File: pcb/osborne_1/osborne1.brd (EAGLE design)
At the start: 40 x 97 mm, 11 parts, among them J2 ATX24RH

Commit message: cleanup
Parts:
- moved JP1 2.24 mm to (6.97, 79.2)
- moved JP2 2.24 mm to (6.97, 67.7)
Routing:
- net +5V: track 69.2 -> 79.6 mm
- net +12V: track 85.0 -> 83.1 mm
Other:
- board text added: "12VDC"
- board text added: "Center Positive"

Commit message: cleanup
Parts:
- moved JP4 0.76 mm to (5.46, 21.2)
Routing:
- net +5V: track 79.6 -> 78.9 mm
- net +12V: track 83.1 -> 82.6 mm
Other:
- board text added: "12V"
- board text added: "5V"
- board text added: "Fan Voltage"
- board text added: "PD1 dekuNukem APR 2023"
- board text removed: "12"
- board text removed: "5"
- board text removed: "PT1 dekuNukem APR 2023"
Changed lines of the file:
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@@
 <grid distance="5" unitdist="mil" unit="mil" style="lines" multiple="1" display="no" altdistance="1" altunitdist="mil" altunit="mil"/>
 <layers>
-<layer number="1" name="Top" color="4" fill="1" visible="no" active="yes"/>
+<layer number="1" name="Top" color="4" fill="1" visible="yes" active="yes"/>
 <layer number="2" name="Route2" color="16" fill="1" visible="no" active="no"/>
 <layer number="3" name="Route3" color="17" fill="1" visible="no" active="no"/>
@@
 <layer number="19" name="Unrouted" color="6" fill="1" visible="yes" active="yes"/>
 <layer number="20" name="Dimension" color="24" fill="1" visible="yes" active="yes"/>
-<layer number="21" name="tPlace" color="7" fill="1" visible="no" active="yes"/>
-<layer number="22" name="bPlace" color="7" fill="1" visible="no" active="yes"/>
-<layer number="23" name="tOrigins" color="15" fill="1" visible="no" active="yes"/>
+<layer number="21" name="tPlace" color="7" fill="1" visible="yes" active="yes"/>
+<layer number="22" name="bPlace" color="7" fill="1" visible="yes" active="yes"/>
+<layer number="23" name="tOrigins" color="15" fill="1" visible="yes" active="yes"/>
 <layer number="24" name="bOrigins" color="15" fill="1" visible="yes" active="yes"/>
-<layer number="25" name="tNames" color="7" fill="1" visible="no" active="yes"/>
-<layer number="26" name="bNames" color="7" fill="1" visible="no" active="yes"/>
-<layer number="27" name="tValues" color="7" fill="1" visible="no" active="yes"/>
-<layer number="28" name="bValues" color="7" fill="1" visible="no" active="yes"/>
+<layer number="25" name="tNames" color="7" fill="1" visible="yes" active="yes"/>
+<layer number="26" name="bNames" color="7" fill="1" visible="yes" active="yes"/>
+<layer number="27" name="tValues" color="7" fill="1" visible="yes" active="yes"/>
+<layer number="28" name="bValues" color="7" fill="1" visible="yes" active="yes"/>
 <layer number="29" name="tStop" color="7" fill="3" visible="no" active="yes"/>
 <layer number="30" name="bStop" color="7" fill="6" visible="no" active="yes"/>
@@
 <layer number="37" name="tTest" color="7" fill="1" visible="no" active="yes"/>
 <layer number="38" name="bTest" color="7" fill="1" visible="no" active="yes"/>
-<layer number="39" name="tKeepout" color="4" fill="11" visible="no" active="yes"/>
+<layer number="39" name="tKeepout" color="4" fill="11" visible="yes" active="yes"/>
 <layer number="40" name="bKeepout" color="1" fill="11" visible="yes" active="yes"/>
-<layer number="41" name="tRestrict" color="4" fill="10" visible="no" active="yes"/>
+<layer number="41" name="tRestrict" color="4" fill="10" visible="yes" active="yes"/>
 <layer number="42" name="bRestrict" color="1" fill="10" visible="yes" active="yes"/>
 <layer number="43" name="vRestrict" color="2" fill="10" visible="no" active="yes"/>
@@
 <layer number="49" name="Reference" color="7" fill="1" visible="no" active="yes"/>
 <layer number="50" name="dxf" color="7" fill="1" visible="no" active="no"/>
-<layer number="51" name="tDocu" color="7" fill="1" visible="no" active="yes"/>
-<layer number="52" name="bDocu" color="7" fill="1" visible="no" active="yes"/>
+<layer number="51" name="tDocu" color="7" fill="1" visible="yes" active="yes"/>
+<layer number="52" name="bDocu" color="7" fill="1" visible="yes" active="yes"/>
 <layer number="53" name="tGND_GNDA" color="7" fill="1" visible="no" active="no"/>
 <layer number="54" name="bGND_GNDA" color="7" fill="1" visible="no" active="no"/>
@@
 <wire x1="0" y1="94.46" x2="0" y2="2.54" width="0" layer="20"/>
 <wire x1="0" y1="2.54" x2="2.54" y2="0" width="0" layer="20" curve="90"/>
-<text x="11.557" y="5.715" size="2.1844" layer="25" distance="35" align="center">picoRC.com</text>
+<text x="11.557" y="5.588" size="2.54" layer="25" distance="35" align="center">picoRC.com</text>
 <text x="28.2636" y="12.5134" size="2.1844" layer="25" distance="35" align="center">Osborne 1
 PicoPSU Adaptor</text>
-<text x="9.922" y="91.722" size="1.4224" layer="25" distance="30" align="center">PT1 dekuNukem
+<text x="9.922" y="91.722" size="1.4224" layer="25" distance="30" align="center">PD1 dekuNukem
 APR 2023</text>
 <text x="4.699" y="50.546" size="1.9304" layer="25" distance="35" rot="R90" align="center">FUSE
@@
 <text x="12.233" y="68.942" size="1.6764" layer="26" rot="MR0" align="center">RED</text>
 <text x="11.725" y="71.482" size="1.6764" layer="26" rot="MR0" align="center">NC</text>
-<text x="1.632" y="18.777" size="1.778" layer="25" align="center">12</text>
-<text x="1.505" y="23.73" size="1.778" layer="25" align="center">5</text>
+<text x="4.845" y="14.967" size="1.778" layer="25" rot="R90" align="center">12V</text>
+<text x="5.442" y="27.07" size="1.778" layer="25" rot="R270" align="center">5V</text>
 <text x="15.132" y="8.363" size="1.778" layer="26" rot="MR90" align="center">GND</text>
 <text x="12.6428" y="8.363" size="1.778" layer="26" rot="MR90" align="center">VCC</text>
@@
 <text x="33.528" y="87.376" size="2.1844" layer="25" distance="35" align="center">Center
 Positive</text>
+<text x="2.667" y="80.391" size="1.778" layer="25" align="center">12V</text>
+<text x="2.667" y="75.438" size="1.778" layer="25" align="center">5V</text>
+<text x="2.667" y="77.851" size="1.778" layer="25" align="center">GND</text>
+<text x="2.667" y="83.058" size="1.778" layer="25" align="center">NC</text>
+<text x="2.667" y="68.961" size="1.778" layer="25" align="center">12V</text>
+<text x="2.667" y="64.008" size="1.778" layer="25" align="center">5V</text>
+<text x="2.667" y="66.421" size="1.778" layer="25" align="center">GND</text>
+<text x="2.667" y="71.628" size="1.778" layer="25" align="center">NC</text>
+<text x="2.14" y="20.847" size="1.778" layer="25" rot="R270" align="center">Fan Voltage</text>
 </plain>
 <attributes>
@@
 <element name="U$2" library="atx_power_control" package="FUSE_HOLDER_3IN1" value="CAR_FUSE_HOLDER3IN1" x="11.43" y="29.591" smashed="yes" rot="R90"/>
 <element name="J2" library="macse" package="ATX24_RIGHT_ANGLE" value="ATX24RH" x="31" y="43" smashed="yes" rot="R90"/>
-<element name="JP4" library="pinhead" library_urn="urn:adsk.eagle:library:325" package="1X03" package3d_urn="urn:adsk.eagle:package:22458/2" value="" x="4.699" y="21.209" smashed="yes" rot="R90">
-<attribute name="POPULARITY" value="92" x="4.699" y="21.209" size="1.778" layer="27" rot="R90" display="off"/>
-<attribute name="VALUE" x="7.874" y="17.399" size="1.27" layer="27" rot="R90"/>
+<element name="JP4" library="pinhead" library_urn="urn:adsk.eagle:library:325" package="1X03" package3d_urn="urn:adsk.eagle:package:22458/2" value="" x="5.461" y="21.209" smashed="yes" rot="R90">
+<attribute name="POPULARITY" value="92" x="5.461" y="21.209" size="1.778" layer="27" rot="R90" display="off"/>
+<attribute name="VALUE" x="8.636" y="17.399" size="1.27" layer="27" rot="R90"/>
 </element>
 <element name="JP3" library="appleii" package="1X04" value="" x="11.303" y="13.716" smashed="yes" rot="MR0"/>
@@
 <wire x1="14.224" y1="40.259" x2="15.494" y2="38.989" width="0.6096" layer="16"/>
 <wire x1="15.494" y1="38.989" x2="15.494" y2="33.655" width="0.6096" layer="16"/>
-<wire x1="5.588" y1="23.749" x2="4.699" y2="23.749" width="0.6096" layer="16"/>
+<wire x1="5.588" y1="23.749" x2="5.461" y2="23.749" width="0.6096" layer="16"/>
 <wire x1="6.096" y1="55.663" x2="6.096" y2="42.037" width="0.6096" layer="16"/>
 <wire x1="15.494" y1="33.655" x2="5.588" y2="23.749" width="0.6096" layer="16"/>
@@
 <contactref element="JP2" pad="3"/>
 <wire x1="9.68" y1="36.641" x2="9.361" y2="36.322" width="1.778" layer="16"/>
-<wire x1="9.361" y1="36.322" x2="2.159" y2="36.322" width="1.778" layer="16"/>
 <wire x1="6.969" y1="80.423" x2="4.937" y2="80.423" width="1.778" layer="16"/>
 <wire x1="13.18" y1="36.641" x2="9.68" y2="36.641" width="1.778" layer="16"/>
-<wire x1="4.699" y1="18.669" x2="2.032" y2="18.669" width="1.016" layer="16"/>
-<wire x1="2.032" y1="18.669" x2="1.778" y2="18.923" width="1.016" layer="16"/>
-<wire x1="1.778" y1="18.923" x2="1.778" y2="35.941" width="1.016" layer="16"/>
-<wire x1="1.778" y1="35.941" x2="1.905" y2="36.068" width="1.016" layer="16"/>
-<wire x1="2.159" y1="36.322" x2="2.905" y2="37.068" width="1.016" layer="16"/>
-<wire x1="1.905" y1="36.068" x2="2.159" y2="36.322" width="1.016" layer="16"/>
 <wire x1="4.937" y1="80.423" x2="2.905" y2="78.391" width="1.778" layer="16"/>
 <wire x1="2.905" y1="78.391" x2="2.905" y2="68.993" width="1.778" layer="16"/>
 <wire x1="2.905" y1="68.993" x2="2.905" y2="37.068" width="1.778" layer="16"/>
 <wire x1="6.969" y1="68.993" x2="2.905" y2="68.993" width="1.778" layer="16"/>
+<wire x1="9.68" y1="36.641" x2="3.332" y2="36.641" width="1.778" layer="16"/>
+<wire x1="3.332" y1="36.641" x2="2.905" y2="37.068" width="1.778" layer="16"/>
+<wire x1="5.461" y1="18.669" x2="3.048" y2="18.669" width="1.016" layer="16"/>
+<wire x1="3.048" y1="18.669" x2="2.286" y2="19.431" width="1.016" layer="16"/>
+<wire x1="2.286" y1="19.431" x2="2.286" y2="36.449" width="1.016" layer="16"/>
+<wire x1="2.286" y1="36.449" x2="2.905" y2="37.068" width="1.016" layer="16"/>
 </signal>
 <signal name="N$2">
 <contactref element="JP3" pad="2"/>
 <contactref element="JP4" pad="2"/>
-<wire x1="4.699" y1="21.209" x2="6.604" y2="21.209" width="1.016" layer="16"/>
-<wire x1="6.604" y1="21.209" x2="12.573" y2="15.24" width="1.016" layer="16"/>
-<wire x1="12.573" y1="15.24" x2="12.573" y2="13.716" width="1.016" layer="16"/>
+<wire x1="5.461" y1="21.209" x2="7.112" y2="21.209" width="1.016" layer="16"/>
+<wire x1="7.112" y1="21.209" x2="12.573" y2="15.748" width="1.016" layer="16"/>
+<wire x1="12.573" y1="15.748" x2="12.573" y2="13.716" width="1.016" layer="16"/>
 </signal>
 <signal name="N$1">

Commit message: finishing touches
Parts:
- added LED1, LED2: (no value), SparkFun-LED:LED_3MM
- added R1, R2: (no value), adafruit:0207/2V
- moved U$2 0.51 mm to (10.9, 29.6)
- moved U$8 0.51 mm to (10.9, 50.8)
- moved JP4 0.25 mm to (5.21, 21.2)
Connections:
- new net N$3: LED1.K, R2.1
- new net N$4: LED2.K, R1.1
- net +12V: now also LED2.A
- net +5V: now also LED1.A
- net GND: now also R1.2, R2.2
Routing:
- net +12V: track 82.6 -> 88.7 mm
- net +5V: track 78.9 -> 82.5 mm
- net N$3: track 0.00 -> 3.30 mm
- net N$4: track 0.00 -> 2.92 mm
- net N$8: track 37.7 -> 38.4 mm
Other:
- board text added: "+"

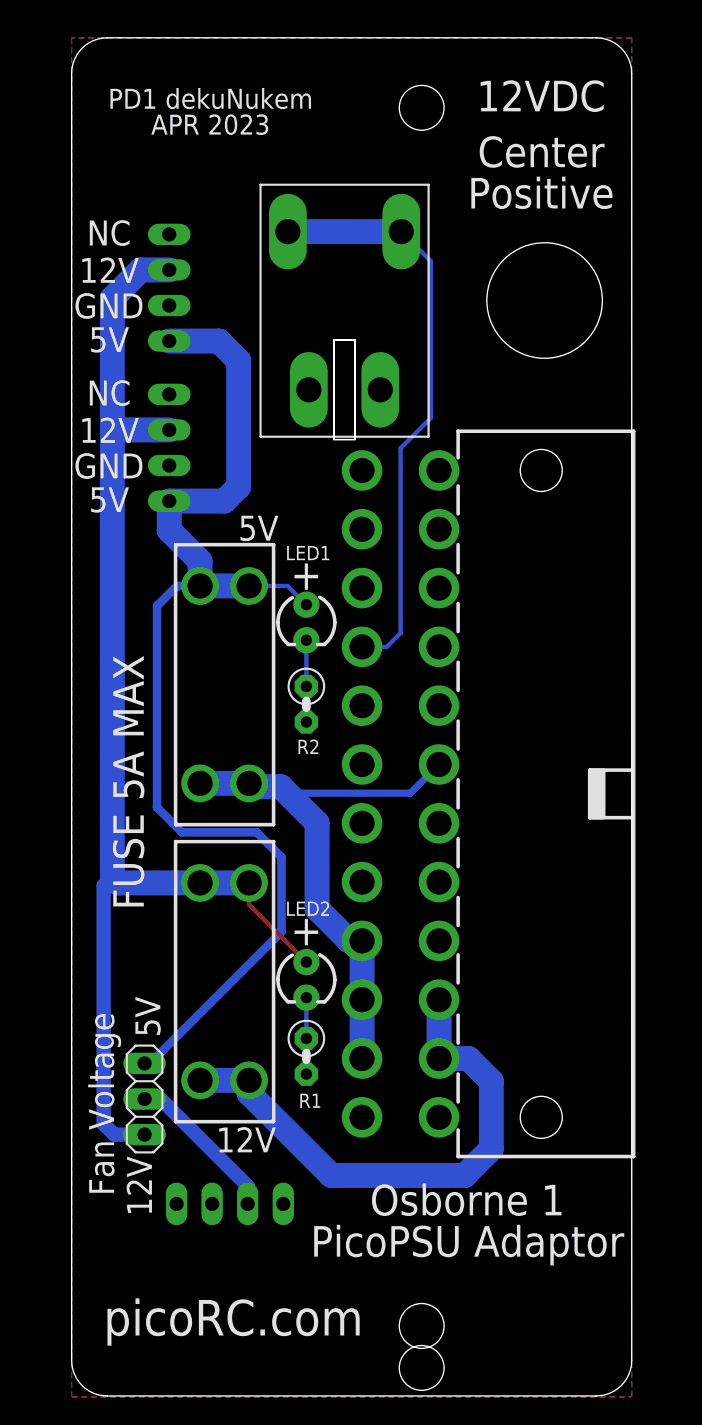
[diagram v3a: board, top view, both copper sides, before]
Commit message: added one more power connector, added decoupling cap
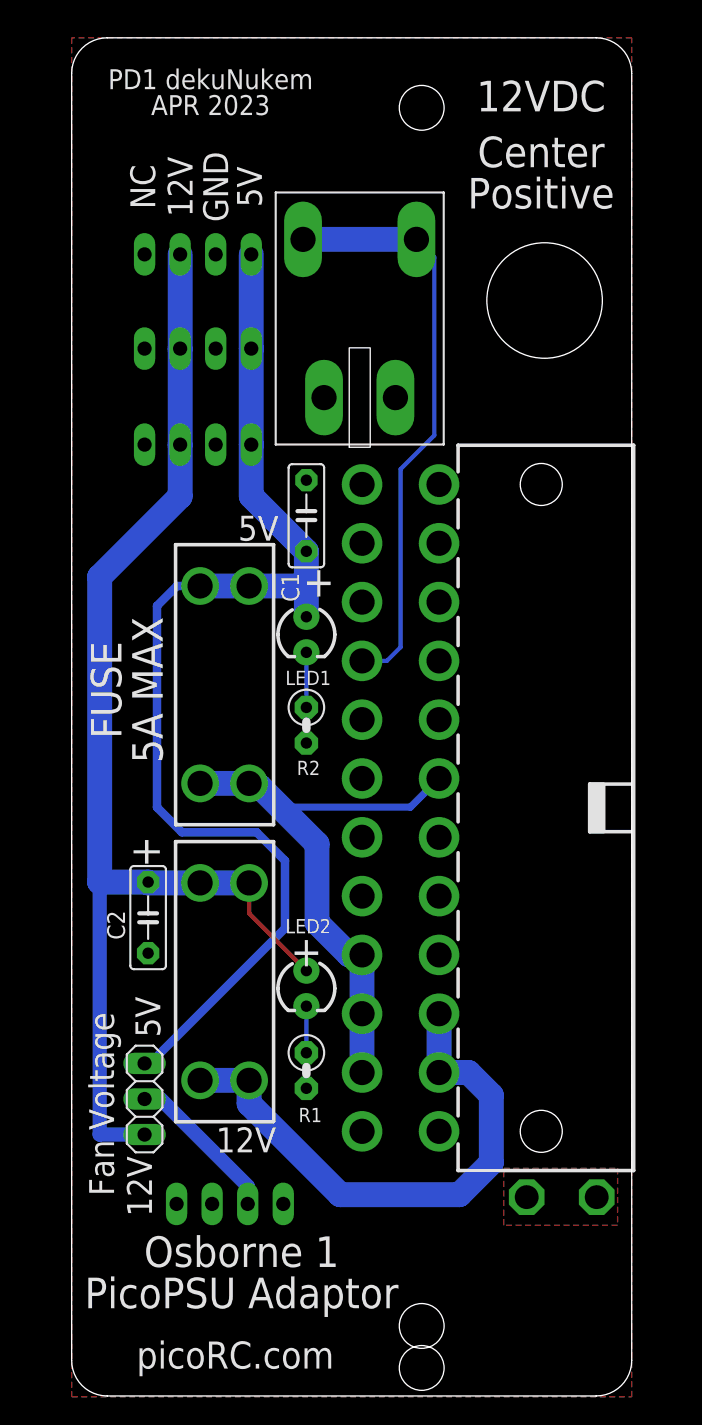
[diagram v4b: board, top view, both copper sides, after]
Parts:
- added C1, C2: (no value), capacitor-wima:C5B2.5
- added JP5: (no value), appleii:1X04
- added TP1, TP2: PTR1PAD1-17, testpad:P1-17
- moved JP2 7.37 mm to (9.02, 74.8), turned to 0 degrees
- moved JP1 3.14 mm to (9.02, 81.5), turned to 0 degrees
- moved R2 1.50 mm to (16.8, 47.9)
- moved U$4 1.22 mm to (20.6, 77.0)
- moved R1 1.02 mm to (16.8, 23.2)
- moved J2 1.00 mm to (31.0, 42.0)
- moved LED1 0.86 mm to (16.8, 54.4)
- moved LED2 0.61 mm to (16.8, 29.1)
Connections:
- net +12V: now also C2.1, JP5.3
- net +5V: now also C1.1, JP5.1
- net GND: now also C1.2, C2.2, JP5.2, TP1.TP, TP2.TP
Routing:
- net +12V: track 88.7 -> 87.1 mm
- net N$8: track 38.4 -> 39.5 mm
- net N$3: track 3.30 -> 3.94 mm
- net N$6: track 42.1 -> 42.6 mm
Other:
- outline, holes or cut-outs redrawn
- board text removed: "RED: 12V ORANGE: GND YELLOW: 5V"

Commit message: changed oritation
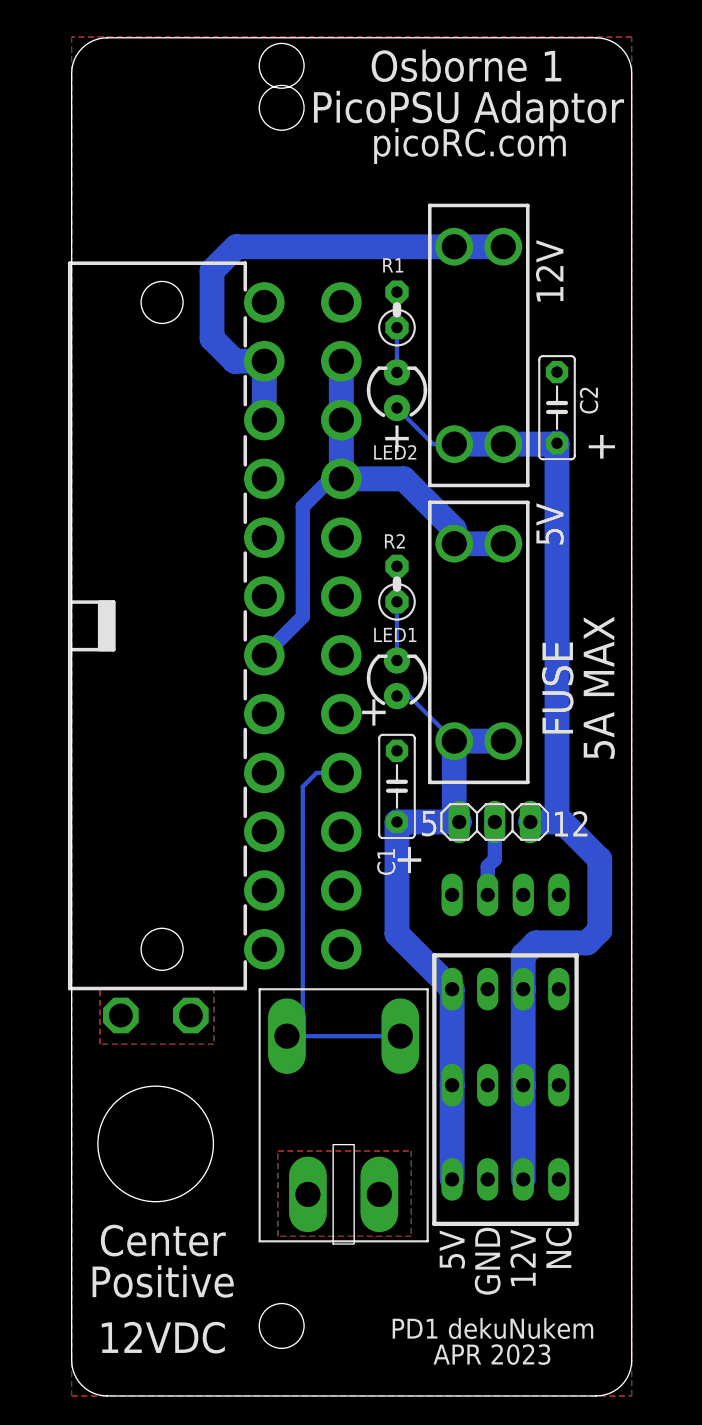
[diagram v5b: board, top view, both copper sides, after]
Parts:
- moved U$5 93.5 mm to (15.0, 95.0), turned to 180 degrees
- moved U$1 87.6 mm to (15.0, 5.00), turned to 180 degrees
- moved U$3 87.6 mm to (15.0, 92.0), turned to 180 degrees
- moved JP1 69.6 mm to (31.0, 15.5), turned to 180 degrees
- moved JP2 57.0 mm to (31.0, 22.2), turned to 180 degrees
- moved U$4 56.9 mm to (19.4, 20.0)
- moved R1 54.7 mm to (23.2, 77.6), turned to 90 degrees
- moved U$2 48.9 mm to (29.1, 75.0), turned to 270 degrees
- moved C2 46.7 mm to (34.7, 70.6), turned to 90 degrees
- moved JP5 44.7 mm to (31.0, 29.1), turned to 180 degrees
- moved LED2 43.2 mm to (23.2, 71.8), turned to 90 degrees
- moved TP2 36.4 mm to (3.52, 27.2), turned to 270 degrees
- moved JP4 31.9 mm to (30.2, 41.0), turned to 180 degrees
- moved JP3 29.6 mm to (31.0, 35.8), turned to 180 degrees
- moved TP1 27.3 mm to (8.52, 27.2), turned to 270 degrees
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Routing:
- net +5V: track 83.0 -> 46.5 mm
- net +12V: track 87.1 -> 72.9 mm
- net N$1: track 41.9 -> 29.6 mm
- net N$2: track 11.2 -> 5.42 mm
- net N$6: track 42.6 -> 37.8 mm
- net N$8: track 39.5 -> 34.9 mm
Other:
- board text added: "12"
- board text added: "5"
- board text added: "FAN"
- board text added: "PWR"
- board text removed: "Fan Voltage"
- board text removed: "PC FAN"

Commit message: changed oritation
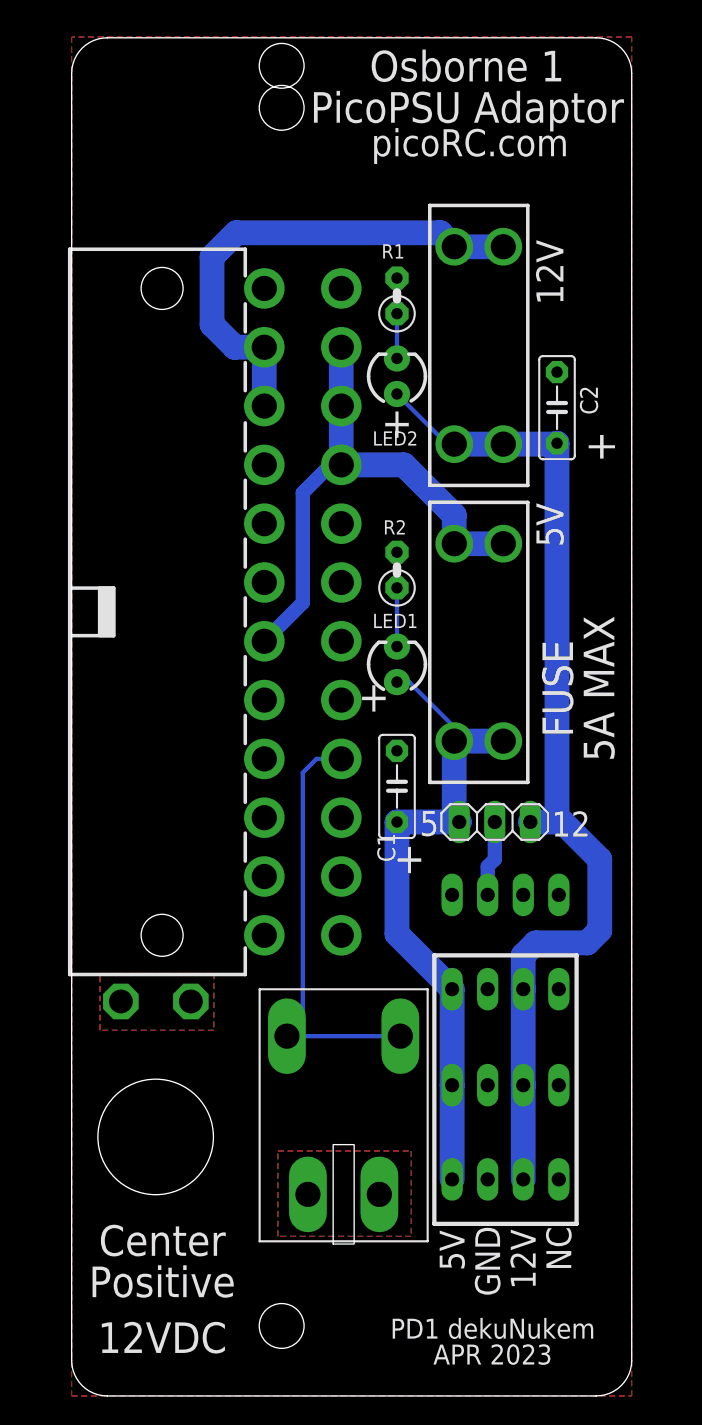
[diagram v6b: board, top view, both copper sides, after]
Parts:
- moved J2 1.00 mm to (9.00, 56.0)
- moved LED1 1.00 mm to (23.2, 52.3)
- moved LED2 1.00 mm to (23.2, 72.8)
- moved R1 1.00 mm to (23.2, 78.6)
- moved R2 1.00 mm to (23.2, 59.0)
- moved TP1 1.00 mm to (8.52, 28.2)
- moved TP2 1.00 mm to (3.52, 28.2)
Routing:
- net N$6: track 37.8 -> 38.8 mm
- net N$1: track 29.6 -> 30.6 mm
- net +5V: track 46.5 -> 47.5 mm
